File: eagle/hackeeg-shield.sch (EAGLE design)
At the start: 141 parts, among them IC1 ADS1299IPAG, IC10 TXB0108PWR, IC11 TXB0108PWR, IC2 TPS72325DBVT, IC3 TPS73225DBVT, IC5 24AA256UID, IC6 TPS60403DBVT, IC7 OPA376DBV, IC8 OPA376DBV, IC9 TXS0102DCUR

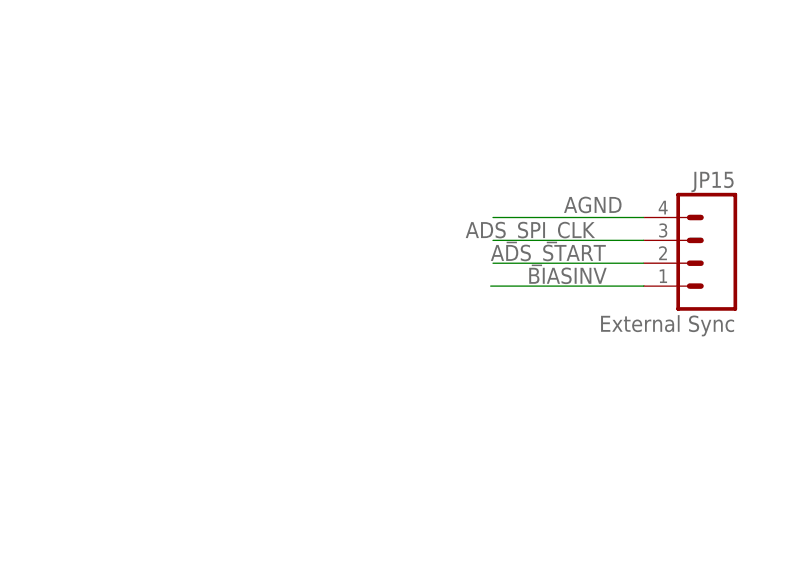
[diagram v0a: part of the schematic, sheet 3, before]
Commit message: add option to put biasout on ext sync connector
- probably won't use this option, saving it just in case
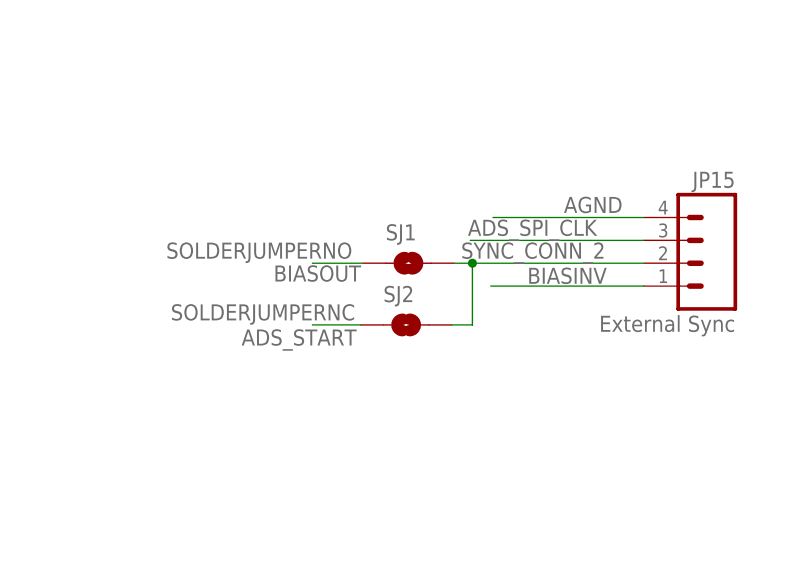
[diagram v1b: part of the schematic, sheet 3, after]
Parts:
- added SJ1: SOLDERJUMPERNO, SparkFun-Passives:SOLDERJUMPERNO
- added SJ2: SOLDERJUMPERNC, SparkFun-Passives:SOLDERJUMPERNC
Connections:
- new net SYNC_CONN_2: JP15.2, SJ1.2, SJ2.2
- net ADS_START: now also SJ2.1; no longer JP15.2
- net BIASOUT: now also SJ1.1
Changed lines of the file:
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@@
 <part name="IC7" library="OPA376" deviceset="OPA376" device="DBV"/>
 <part name="TP4" library="adafruit" deviceset="PINHD-1X1" device="" value="VREFP_TEST_POINT"/>
+<part name="SJ1" library="SparkFun-Passives" deviceset="SOLDERJUMPER" device="NO"/>
+<part name="SJ2" library="SparkFun-Passives" deviceset="SOLDERJUMPER" device="NC"/>
 </parts>
 <sheets>
@@
 </instance>
 <instance part="JP15" gate="G$1" x="283.718" y="56.388" rot="MR0"/>
+<instance part="SJ1" gate="1" x="252.476" y="56.388" smashed="yes">
+<attribute name="NAME" x="249.936" y="58.928" size="1.778" layer="95"/>
+<attribute name="VALUE" x="225.552" y="56.896" size="1.778" layer="96"/>
+</instance>
+<instance part="SJ2" gate="1" x="252.222" y="49.53" smashed="yes">
+<attribute name="NAME" x="249.682" y="52.07" size="1.778" layer="95"/>
+<attribute name="VALUE" x="226.06" y="50.038" size="1.778" layer="96"/>
+</instance>
 </instances>
 <busses>
@@
 </segment>
 <segment>
-<wire x1="278.638" y1="58.928" x2="261.874" y2="58.928" width="0.1524" layer="91"/>
-<label x="258.826" y="59.182" size="1.778" layer="95"/>
+<wire x1="278.638" y1="58.928" x2="259.334" y2="58.928" width="0.1524" layer="91"/>
 <pinref part="JP15" gate="G$1" pin="3"/>
+<label x="259.08" y="59.436" size="1.778" layer="95"/>
 </segment>
 </net>
@@
 </segment>
 <segment>
-<wire x1="278.638" y1="56.388" x2="261.874" y2="56.388" width="0.1524" layer="91"/>
-<label x="261.62" y="56.642" size="1.778" layer="95"/>
-<pinref part="JP15" gate="G$1" pin="2"/>
+<pinref part="SJ2" gate="1" pin="1"/>
+<label x="233.934" y="47.244" size="1.778" layer="95"/>
+<wire x1="247.142" y1="49.53" x2="241.808" y2="49.53" width="0.1524" layer="91"/>
 </segment>
 </net>
@@
 </segment>
 </net>
+<net name="SYNC_CONN_2" class="0">
+<segment>
+<wire x1="278.638" y1="56.388" x2="259.588" y2="56.388" width="0.1524" layer="91"/>
+<label x="258.318" y="56.896" size="1.778" layer="95"/>
+<pinref part="JP15" gate="G$1" pin="2"/>
+<pinref part="SJ1" gate="1" pin="2"/>
+<wire x1="257.556" y1="56.388" x2="259.588" y2="56.388" width="0.1524" layer="91"/>
+<pinref part="SJ2" gate="1" pin="2"/>
+<wire x1="257.302" y1="49.53" x2="259.588" y2="49.53" width="0.1524" layer="91"/>
+<wire x1="259.588" y1="49.53" x2="259.588" y2="56.388" width="0.1524" layer="91"/>
+<junction x="259.588" y="56.388"/>
+</segment>
+</net>
+<net name="BIASOUT" class="0">
+<segment>
+<pinref part="SJ1" gate="1" pin="1"/>
+<wire x1="247.396" y1="56.388" x2="241.808" y2="56.388" width="0.1524" layer="91"/>
+<label x="237.49" y="54.356" size="1.778" layer="95"/>
+</segment>
+</net>
